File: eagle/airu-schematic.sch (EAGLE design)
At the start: 16 parts, among them U1 BMP180, U2 DHT22, U3 GPS

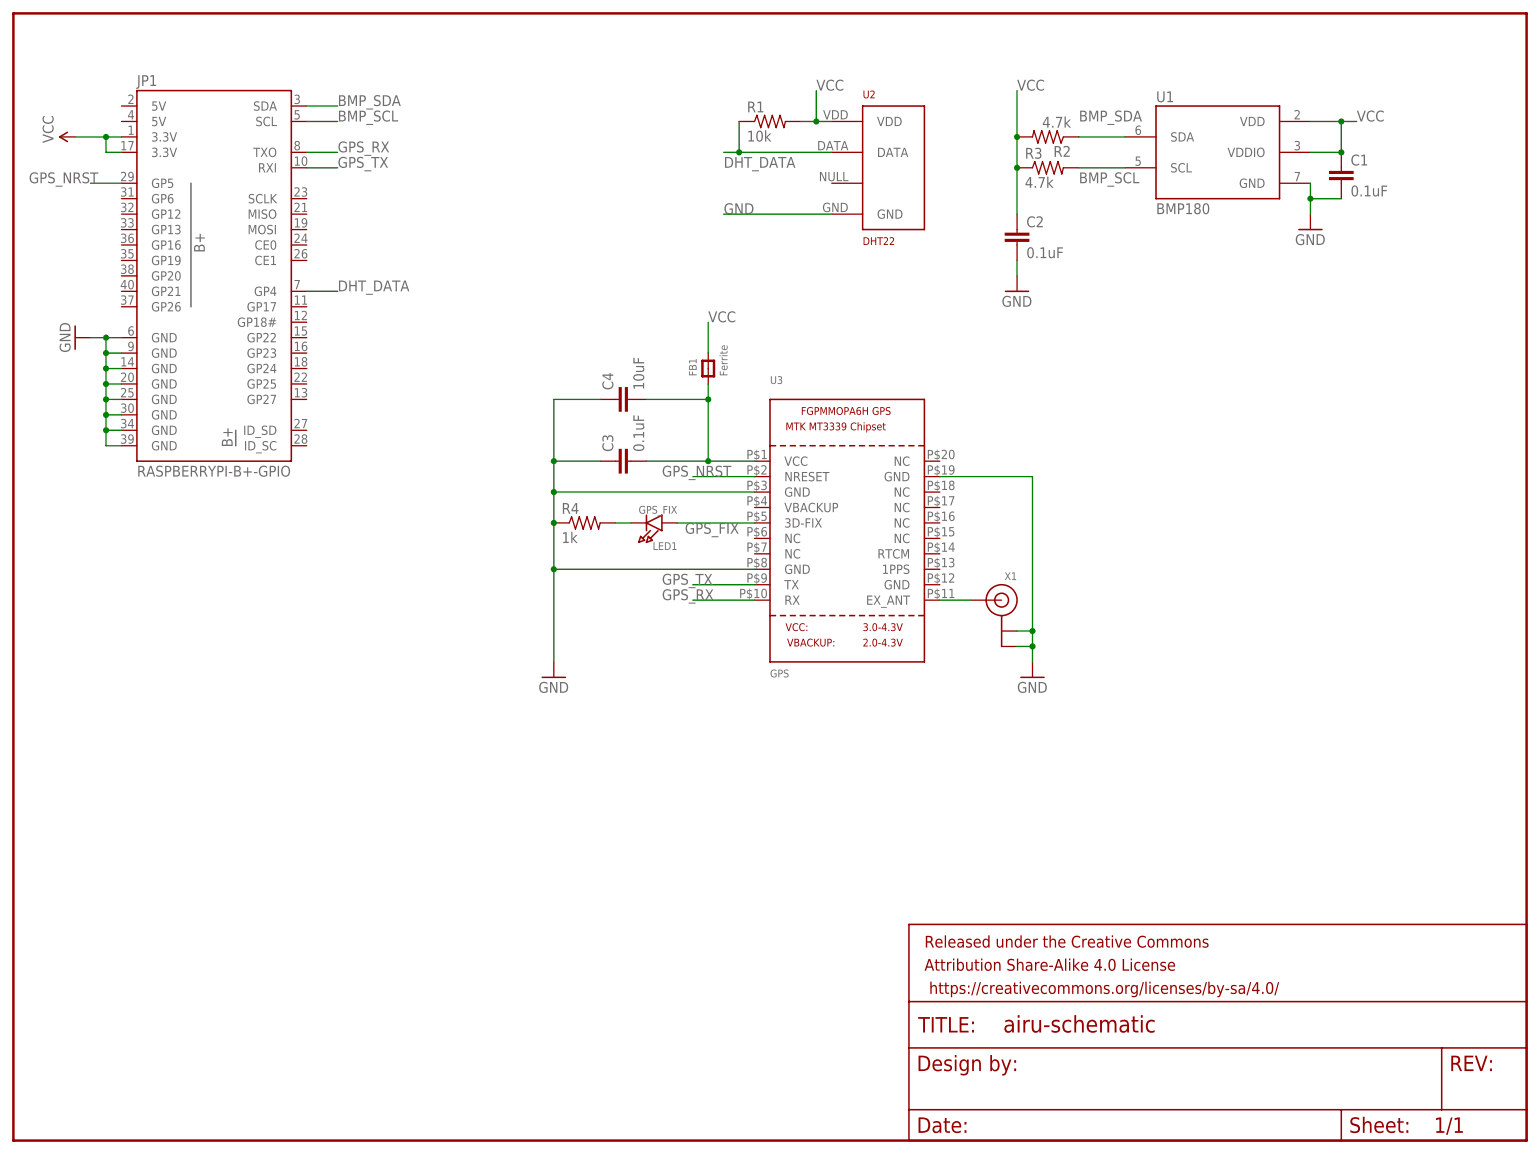
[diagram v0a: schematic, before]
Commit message: Added MCP3008 ADC to the schematic, and BOM.
This commit adds an MCP3008 ADC to the schematic, which is used for
converting the analog sensor values to a digital sequence. This commit
also includes a preliminary Bill of Materials that will be used to order
components in bulk for assembly (post fabrication).
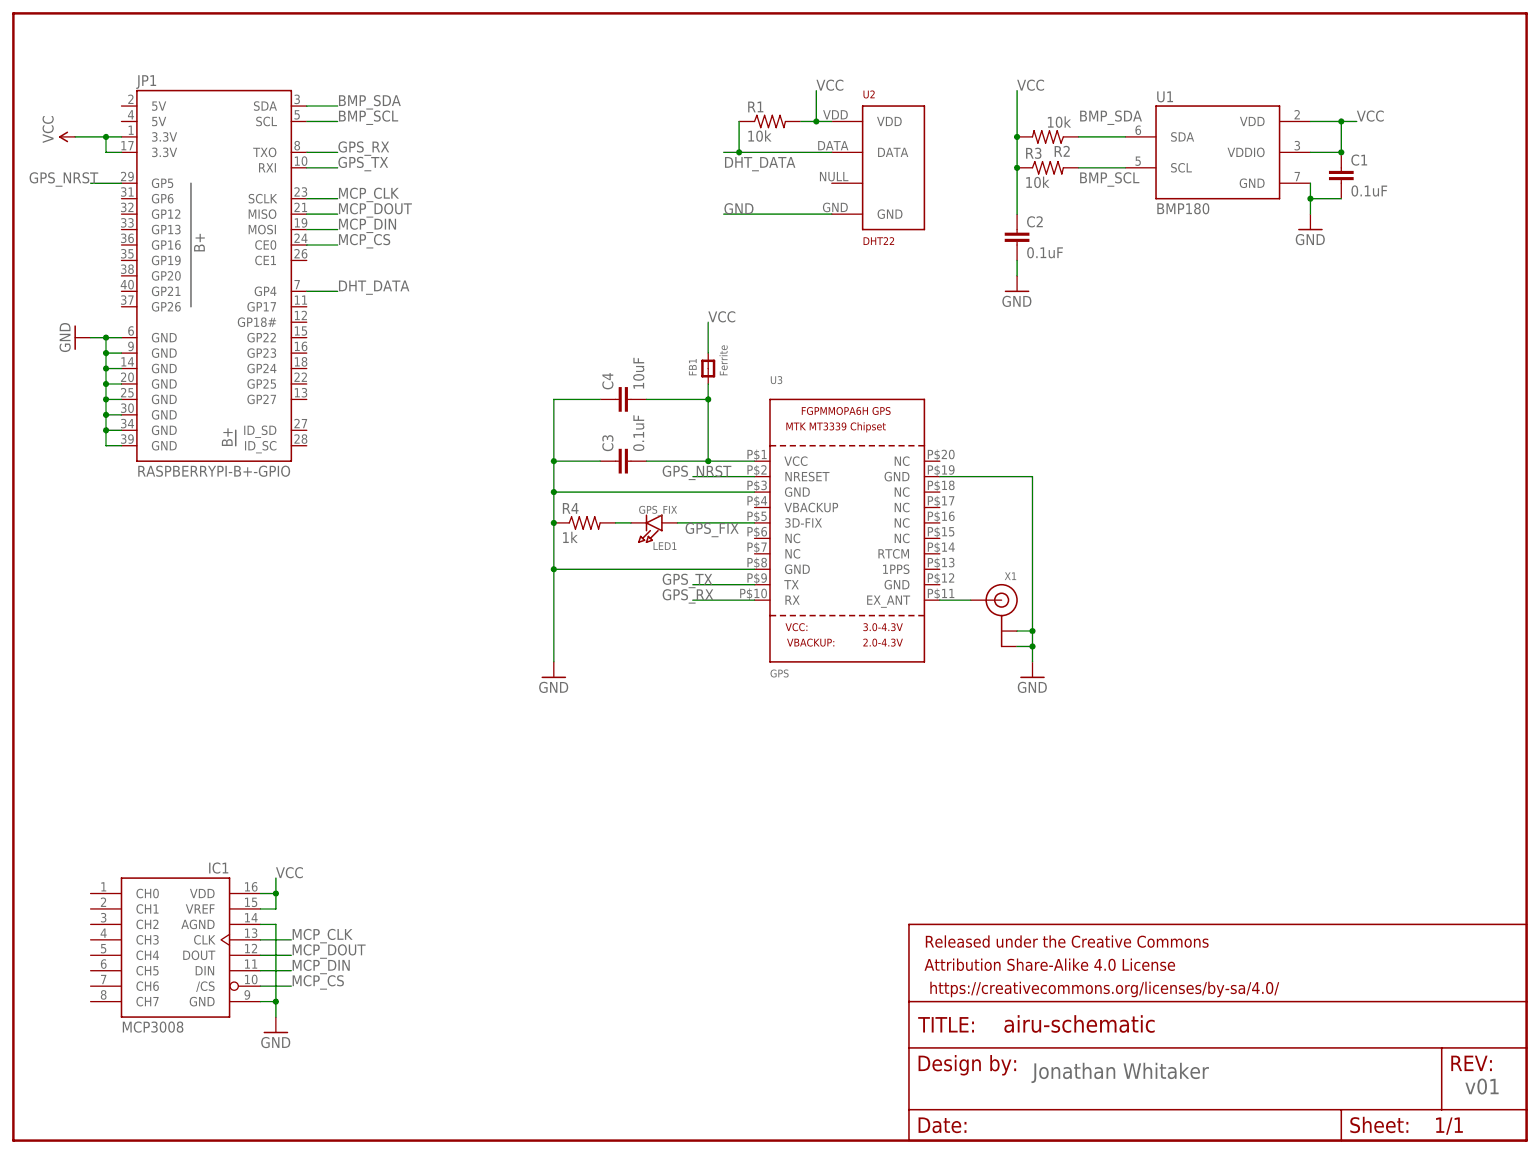
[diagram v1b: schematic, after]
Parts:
- added IC1: MCP3008, adafruit:MCP3008
- R2, R3: value 4.7k -> 10k
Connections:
- new net MCP_CLK: IC1.CLK, JP1.SCLK
- new net MCP_CS: IC1./CS, JP1.CE0
- new net MCP_DIN: IC1.DIN, JP1.MOSI
- new net MCP_DOUT: IC1.DOUT, JP1.MISO
- net GND: now also IC1.AGND, IC1.GND
- net VCC: now also IC1.VDD, IC1.VREF
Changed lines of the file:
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@@
 <?xml version="1.0" encoding="utf-8"?>
 <!DOCTYPE eagle SYSTEM "eagle.dtd">
-<eagle version="7.2.0">
+<eagle version="7.1.0">
 <drawing>
 <settings>
@@
 <layer number="56" name="wert" color="7" fill="1" visible="no" active="no"/>
 <layer number="57" name="tCAD" color="7" fill="1" visible="no" active="no"/>
+<layer number="59" name="tCarbon" color="7" fill="1" visible="no" active="no"/>
+<layer number="60" name="bCarbon" color="7" fill="1" visible="no" active="no"/>
 <layer number="90" name="Modules" color="5" fill="1" visible="yes" active="yes"/>
 <layer number="91" name="Nets" color="2" fill="1" visible="yes" active="yes"/>
@@
 <layer number="127" name="_tValues" color="7" fill="1" visible="yes" active="yes"/>
 <layer number="128" name="_bValues" color="7" fill="1" visible="yes" active="yes"/>
+<layer number="129" name="Mask" color="7" fill="1" visible="yes" active="yes"/>
 <layer number="131" name="tAdjust" color="7" fill="1" visible="yes" active="yes"/>
 <layer number="132" name="bAdjust" color="7" fill="1" visible="yes" active="yes"/>
@@
 <layer number="223" name="223bmp" color="24" fill="1" visible="no" active="no"/>
 <layer number="224" name="224bmp" color="25" fill="1" visible="no" active="no"/>
+<layer number="225" name="225bmp" color="7" fill="1" visible="yes" active="yes"/>
+<layer number="226" name="226bmp" color="7" fill="1" visible="yes" active="yes"/>
+<layer number="227" name="227bmp" color="7" fill="1" visible="yes" active="yes"/>
+<layer number="228" name="228bmp" color="7" fill="1" visible="yes" active="yes"/>
+<layer number="229" name="229bmp" color="7" fill="1" visible="yes" active="yes"/>
+<layer number="230" name="230bmp" color="7" fill="1" visible="yes" active="yes"/>
 <layer number="231" name="Eagle3D_PG1" color="7" fill="1" visible="no" active="no"/>
 <layer number="232" name="Eagle3D_PG2" color="7" fill="1" visible="no" active="no"/>
@@
 <layer number="251" name="SMDround" color="12" fill="11" visible="no" active="no"/>
 <layer number="254" name="cooling" color="7" fill="1" visible="yes" active="yes"/>
+<layer number="255" name="routoute" color="7" fill="1" visible="yes" active="yes"/>
 </layers>
 <schematic xreflabel="%F%N/%S.%C%R" xrefpart="/%S.%C%R">
@@
 <part name="C1" library="SparkFun-Passives" deviceset="CAP" device="1206" value="0.1uF"/>
 <part name="GND2" library="SparkFun-Aesthetics" deviceset="GND" device=""/>
-<part name="R2" library="SparkFun-Passives" deviceset="RESISTOR" device="1206" value="4.7k"/>
-<part name="R3" library="SparkFun-Passives" deviceset="RESISTOR" device="1206" value="4.7k"/>
+<part name="R2" library="SparkFun-Passives" deviceset="RESISTOR" device="1206" value="10k"/>
+<part name="R3" library="SparkFun-Passives" deviceset="RESISTOR" device="1206" value="10k"/>
 <part name="C2" library="SparkFun-Passives" deviceset="CAP" device="1206" value="0.1uF"/>
 <part name="GND3" library="SparkFun-Aesthetics" deviceset="GND" device=""/>
@@
 <part name="LED1" library="microbuilder" deviceset="LED" device="1206" value="GPS_FIX"/>
 <part name="C4" library="SparkFun-Passives" deviceset="CAP" device="1206" value="10uF"/>
+<part name="IC1" library="adafruit" deviceset="MCP3008" device=""/>
+<part name="GND6" library="SparkFun-Aesthetics" deviceset="GND" device=""/>
 </parts>
 <sheets>
@@
 <instance part="FRAME1" gate="G$1" x="0" y="0"/>
 <instance part="FRAME1" gate="V" x="147.32" y="0">
-<attribute name="DESIGNER" x="147.32" y="0" size="1.778" layer="96" display="off"/>
+<attribute name="DESIGNER" x="167.64" y="10.16" size="2.54" layer="96"/>
+<attribute name="VERSION" x="238.76" y="7.62" size="2.54" layer="96"/>
 </instance>
 <instance part="JP1" gate="G$1" x="33.02" y="144.78"/>
@@
 <instance part="LED1" gate="G$1" x="104.14" y="101.6" rot="R180"/>
 <instance part="C4" gate="G$1" x="101.6" y="121.92" rot="R90"/>
+<instance part="IC1" gate="G$1" x="25.4" y="33.02"/>
+<instance part="GND6" gate="1" x="43.18" y="17.78"/>
 </instances>
 <busses>
@@
 <junction x="88.9" y="111.76"/>
 </segment>
+<segment>
+<pinref part="IC1" gate="G$1" pin="AGND"/>
+<wire x1="40.64" y1="35.56" x2="43.18" y2="35.56" width="0.1524" layer="91"/>
+<wire x1="43.18" y1="35.56" x2="43.18" y2="22.86" width="0.1524" layer="91"/>
+<pinref part="IC1" gate="G$1" pin="GND"/>
+<wire x1="43.18" y1="22.86" x2="40.64" y2="22.86" width="0.1524" layer="91"/>
+<wire x1="43.18" y1="22.86" x2="43.18" y2="20.32" width="0.1524" layer="91"/>
+<junction x="43.18" y="22.86"/>
+<pinref part="GND6" gate="1" pin="GND"/>
+</segment>
 </net>
 <net name="VCC" class="0">
@@
 <wire x1="114.3" y1="129.54" x2="114.3" y2="134.62" width="0.1524" layer="91"/>
 <label x="114.3" y="134.62" size="1.778" layer="95"/>
+</segment>
+<segment>
+<pinref part="IC1" gate="G$1" pin="VDD"/>
+<wire x1="40.64" y1="40.64" x2="43.18" y2="40.64" width="0.1524" layer="91"/>
+<wire x1="43.18" y1="40.64" x2="43.18" y2="38.1" width="0.1524" layer="91"/>
+<pinref part="IC1" gate="G$1" pin="VREF"/>
+<wire x1="43.18" y1="38.1" x2="40.64" y2="38.1" width="0.1524" layer="91"/>
+<wire x1="43.18" y1="40.64" x2="43.18" y2="43.18" width="0.1524" layer="91"/>
+<junction x="43.18" y="40.64"/>
+<label x="43.18" y="43.18" size="1.778" layer="95"/>
 </segment>
 </net>
@@
 </segment>
 </net>
+<net name="MCP_CLK" class="0">
+<segment>
+<pinref part="IC1" gate="G$1" pin="CLK"/>
+<wire x1="40.64" y1="33.02" x2="45.72" y2="33.02" width="0.1524" layer="91"/>
+<label x="45.72" y="33.02" size="1.778" layer="95"/>
+</segment>
+<segment>
+<pinref part="JP1" gate="G$1" pin="SCLK"/>
+<wire x1="48.26" y1="154.94" x2="53.34" y2="154.94" width="0.1524" layer="91"/>
+<label x="53.34" y="154.94" size="1.778" layer="95"/>
+</segment>
+</net>
+<net name="MCP_DOUT" class="0">
+<segment>
+<pinref part="IC1" gate="G$1" pin="DOUT"/>
+<wire x1="40.64" y1="30.48" x2="45.72" y2="30.48" width="0.1524" layer="91"/>
+<label x="45.72" y="30.48" size="1.778" layer="95"/>
+</segment>
+<segment>
+<pinref part="JP1" gate="G$1" pin="MISO"/>
+<wire x1="48.26" y1="152.4" x2="53.34" y2="152.4" width="0.1524" layer="91"/>
+<label x="53.34" y="152.4" size="1.778" layer="95"/>
+</segment>
+</net>
+<net name="MCP_DIN" class="0">
+<segment>
+<pinref part="IC1" gate="G$1" pin="DIN"/>
+<wire x1="40.64" y1="27.94" x2="45.72" y2="27.94" width="0.1524" layer="91"/>
+<label x="45.72" y="27.94" size="1.778" layer="95"/>
+</segment>
+<segment>
+<pinref part="JP1" gate="G$1" pin="MOSI"/>
+<wire x1="48.26" y1="149.86" x2="53.34" y2="149.86" width="0.1524" layer="91"/>
+<label x="53.34" y="149.86" size="1.778" layer="95"/>
+</segment>
+</net>
+<net name="MCP_CS" class="0">
+<segment>
+<pinref part="IC1" gate="G$1" pin="/CS"/>
+<wire x1="40.64" y1="25.4" x2="45.72" y2="25.4" width="0.1524" layer="91"/>
+<label x="45.72" y="25.4" size="1.778" layer="95"/>
+</segment>
+<segment>
+<pinref part="JP1" gate="G$1" pin="CE0"/>
+<wire x1="48.26" y1="147.32" x2="53.34" y2="147.32" width="0.1524" layer="91"/>
+<label x="53.34" y="147.32" size="1.778" layer="95"/>
+</segment>
+</net>

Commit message: Added the MQ-7 circuit and supporting code.
This commit adds the MQ-7 circuit to the airU board schematic. It
also includes the supporting code needed to read from the sensor.
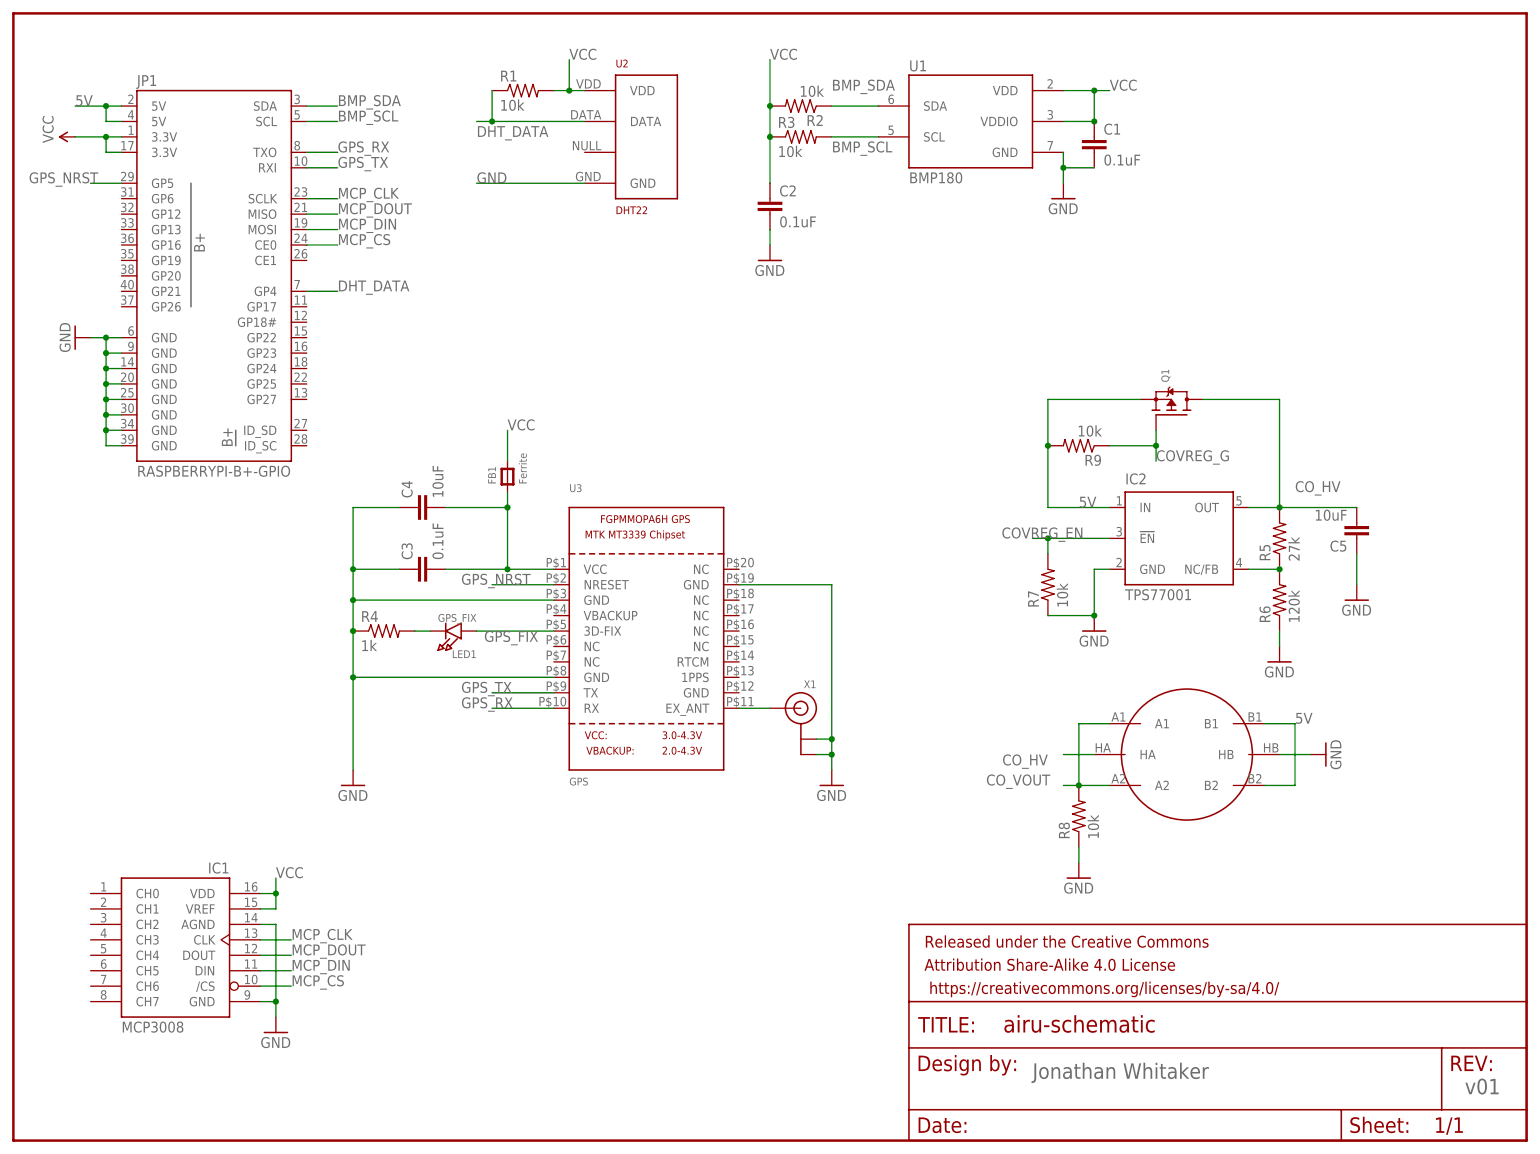
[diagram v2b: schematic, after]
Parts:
- added C5: 10uF, SparkFun-Passives:CAP1206
- added IC2: TPS77001, texas:TPS77001
- added Q1: (no value), microbuilder:MOSFET-P
- added R5: 27k, SparkFun-Passives:RESISTOR1206
- added R6: 120k, SparkFun-Passives:RESISTOR1206
- added R7, R8, R9: 10k, SparkFun-Passives:RESISTOR1206
- added U$1: METHANE_SENSOR, SparkFun-Sensors:METHANE_SENSOR
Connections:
- new net 5V: IC2.IN, JP1.5V@2, JP1.5V@4, Q1.S, R9.2, U$1.B1, U$1.B2
- new net COVREG_EN: IC2.!EN, R7.2
- new net COVREG_G: Q1.G, R9.1
- new net CO_HV: C5.2, IC2.OUT, Q1.D, R5.2, U$1.HA
- new net CO_VOUT: R8.2, U$1.A1, U$1.A2
- new net N$5: IC2.NC/FB, R5.1, R6.2
- net GND: now also C5.1, IC2.GND, R6.1, R7.1, R8.1, U$1.HB
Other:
- note added: "MQ-7 CO"
- moved on the sheet: C1, C2, C3, C4, FB1, LED1, R1, R2, R3, R4, U1, U2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
